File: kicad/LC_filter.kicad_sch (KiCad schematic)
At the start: 16 parts

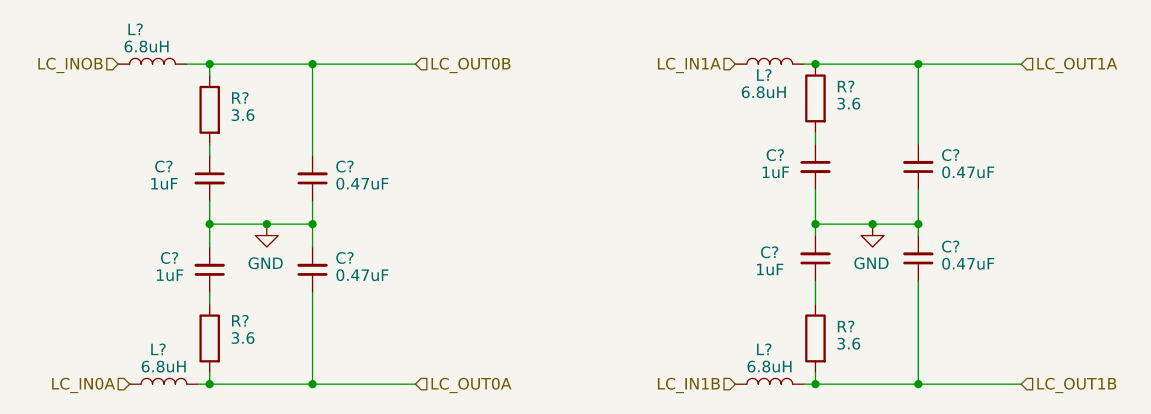
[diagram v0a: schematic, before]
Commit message: changed schematic layout
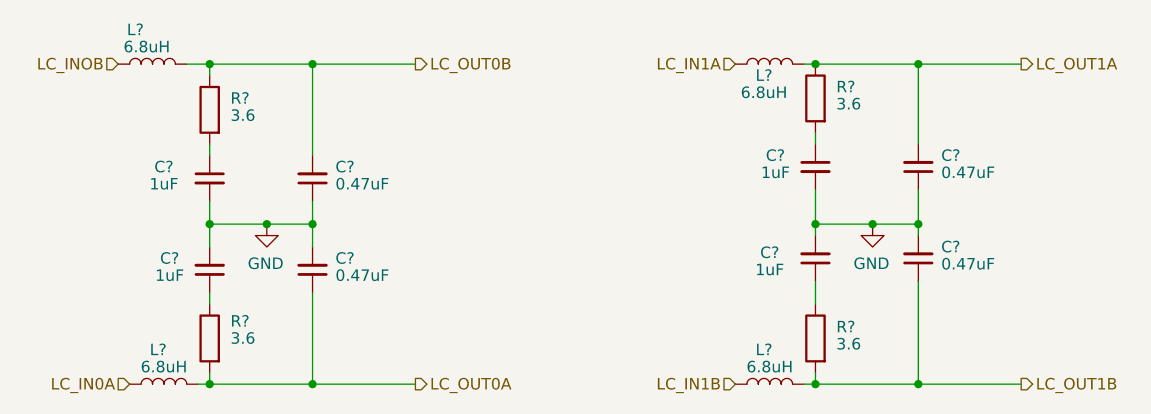
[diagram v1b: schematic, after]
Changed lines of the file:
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@@
     (stroke (width 0) (type default) (color 0 0 0 0))
   )
-  (hierarchical_label "LC_OUT0A" (shape input) (at 109.22 80.01 0)
+  (hierarchical_label "LC_OUT0A" (shape output) (at 109.22 80.01 0)
     (effects (font (size 1.27 1.27)) (justify left))
   )
-  (hierarchical_label "LC_OUT1A" (shape input) (at 176.53 44.45 0)
+  (hierarchical_label "LC_OUT1A" (shape output) (at 176.53 44.45 0)
     (effects (font (size 1.27 1.27)) (justify left))
   )
@@
     (effects (font (size 1.27 1.27)) (justify right))
   )
-  (hierarchical_label "LC_OUT1B" (shape input) (at 176.53 80.01 0)
+  (hierarchical_label "LC_OUT1B" (shape output) (at 176.53 80.01 0)
     (effects (font (size 1.27 1.27)) (justify left))
   )
@@
     (effects (font (size 1.27 1.27)) (justify right))
   )
-  (hierarchical_label "LC_OUT0B" (shape input) (at 109.22 44.45 0)
+  (hierarchical_label "LC_OUT0B" (shape output) (at 109.22 44.45 0)
     (effects (font (size 1.27 1.27)) (justify left))
   )
